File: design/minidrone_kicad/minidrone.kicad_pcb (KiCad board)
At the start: 2 copper layers, 40.6 x 73.7 mm, 34 parts, among them J1 programming, J2 HM-13 Bluetooth, J3 BAT, J4 mpu6050, J5 FL Motor, J6 BL Motor, J7 FR Motor, J8 BR Motor, Q1 SI2302, Q2 SI2302, Q3 SI2302, Q4 SI2302, U1 stm32_BluePill

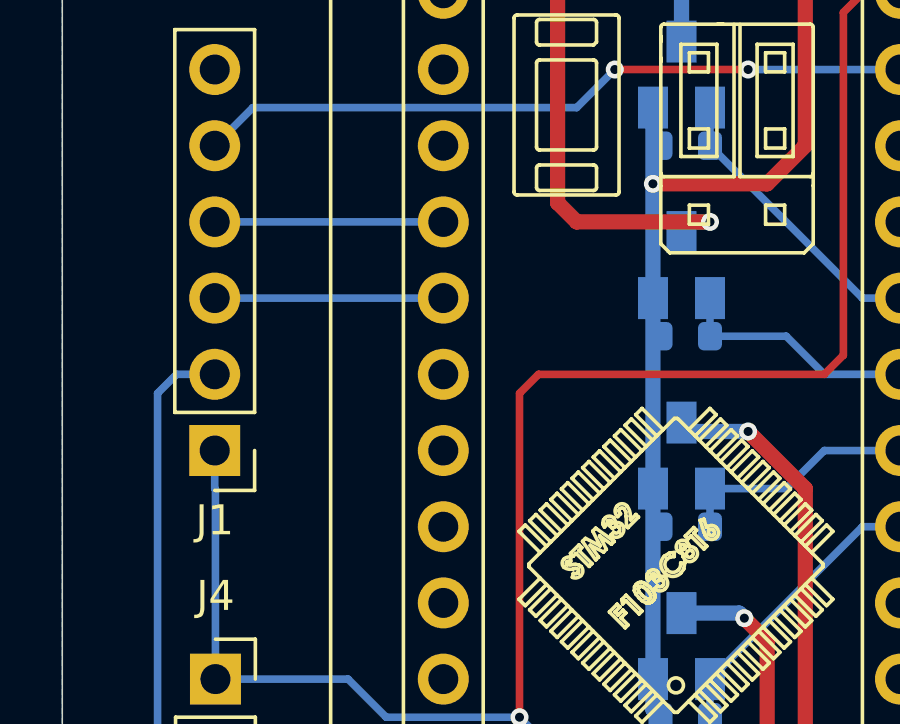
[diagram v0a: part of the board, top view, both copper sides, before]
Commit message: fix(PCH/PCB): Programming pins and motor pins definition.
Correct the programming TX/RX connection.
Update the motor net-names due to the design changed.
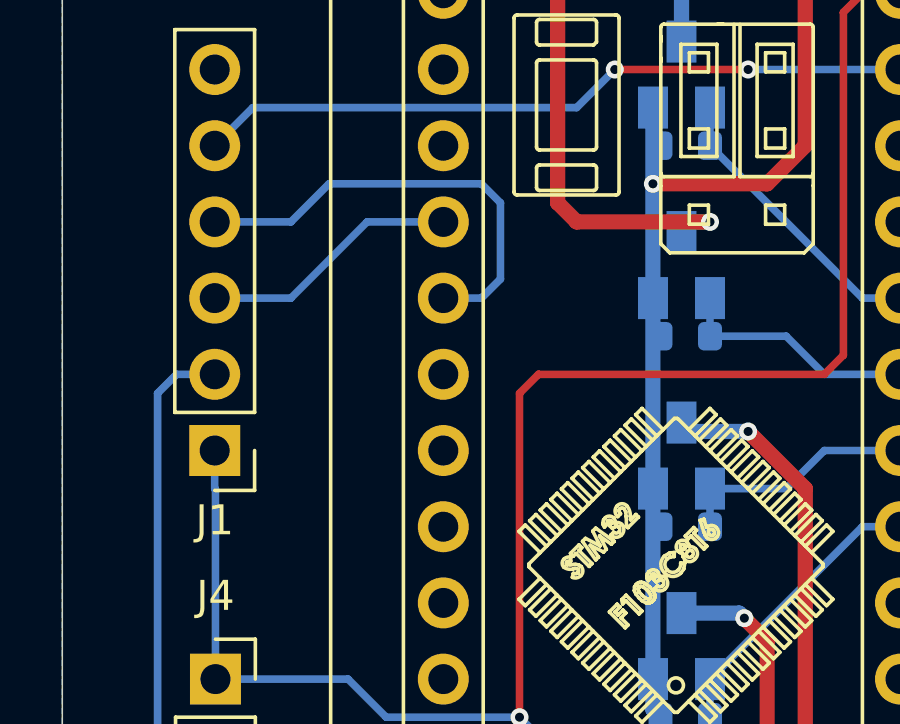
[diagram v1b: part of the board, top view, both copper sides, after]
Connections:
- J1 pad 3: /PRG_TX -> /PRG_RX
- J1 pad 4: /PRG_RX -> /PRG_TX
- Q1 pad 1: /FL_PWM -> /BR_PWM
- Q2 pad 1: /BL_PWM -> /FR_PWM
- Q3 pad 1: /FR_PWM -> /BL_PWM
- Q4 pad 1: /BR_PWM -> /FL_PWM
- R10 pad 1: /FR_PWM -> /BL_PWM
- R11 pad 1: /BR_PWM -> /FL_PWM
- R8 pad 1: /FL_PWM -> /BR_PWM
- R9 pad 1: /BL_PWM -> /FR_PWM
- U1 pad 31: /BL_PWM -> /FR_PWM
- U1 pad 32: /FR_PWM -> /BL_PWM
- U1 pad 33: /FL_PWM -> /BR_PWM
- U1 pad 34: /BR_PWM -> /FL_PWM
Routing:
- net /PRG_TX: track 7.62 -> 15.0 mm
- net /FL_PWM: track 8.15 -> 9.72 mm
- net /BR_PWM: track 9.72 -> 8.15 mm
- net /FR_PWM: track 8.15 -> 9.72 mm
- net /BL_PWM: track 9.72 -> 8.15 mm
- net /PRG_RX: track 7.62 -> 8.67 mm

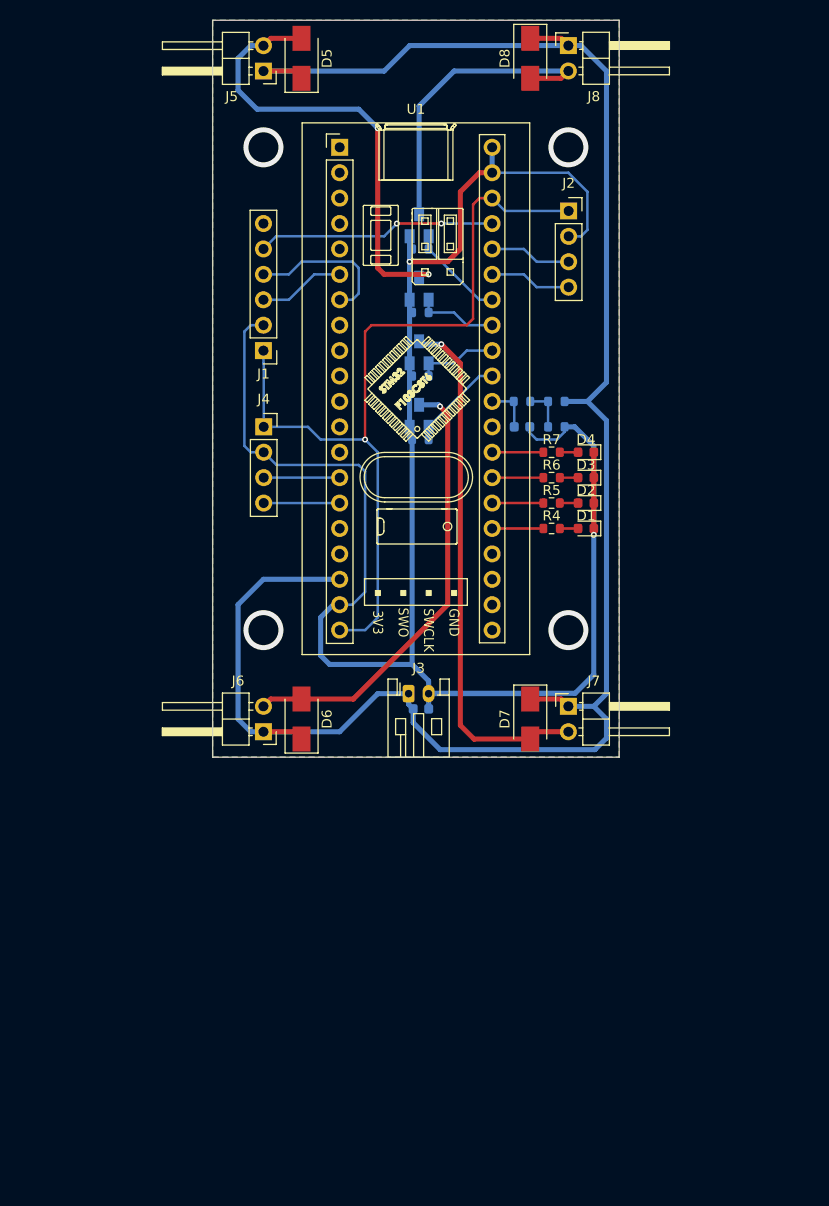
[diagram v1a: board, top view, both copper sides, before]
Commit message: docs(SCH/PCB): Update the PCB design to v2.
The v1's handmade version is too heavy.
 - Remove the STM32 blue pill board.
 - Using the STM32F103CBT6 to make sure the ROM size enough.
 - Design the PCB as the drone's frame.
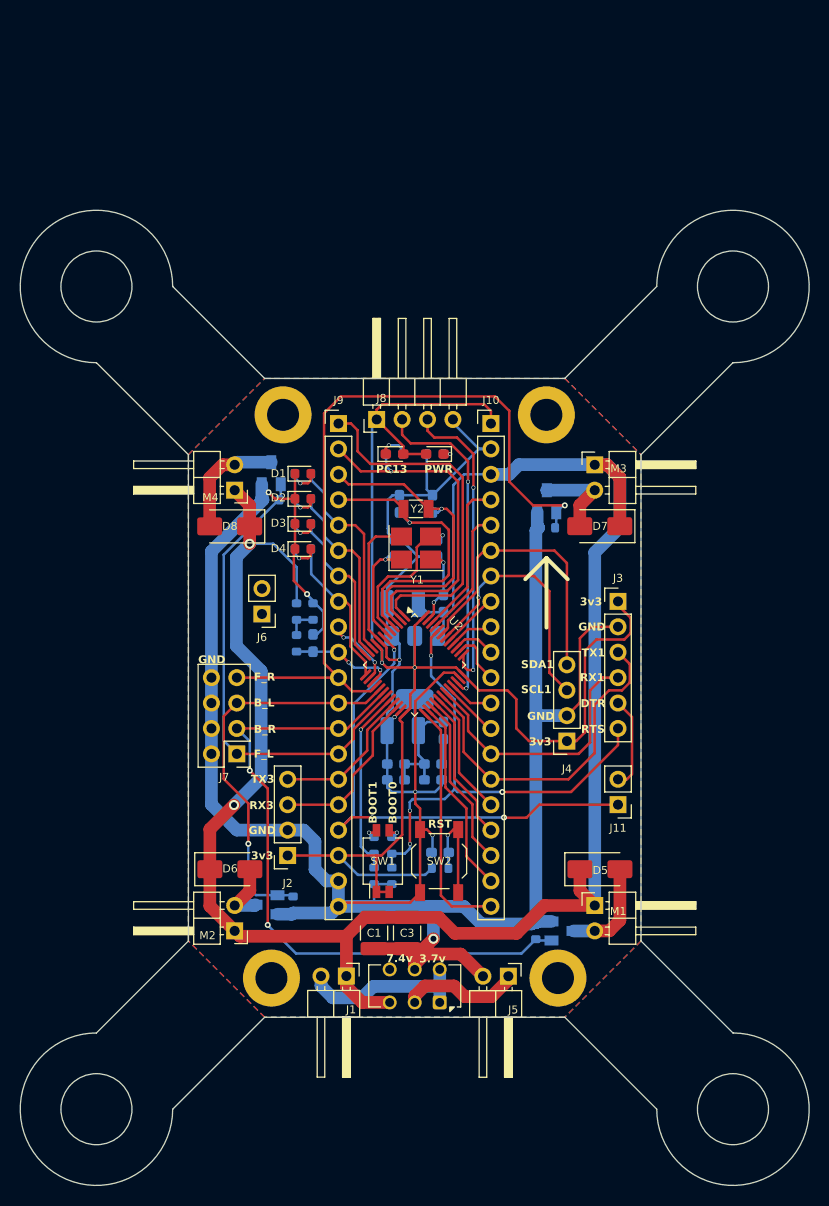
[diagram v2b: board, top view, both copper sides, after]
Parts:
- added ?: , , F.Cu at (135.7, 131.5)
- added ?: , , F.Cu at (163.3, 75.0)
- added ?: , , F.Cu at (164.3, 131.3)
- added C10: 0.1 uF, Capacitor_SMD:C_0603_1608Metric_Pad1.08x0.95mm_HandSolder, B.Cu at (148.1, 111.5)
- added C11: 0.1 uF, Capacitor_SMD:C_0603_1608Metric_Pad1.08x0.95mm_HandSolder, B.Cu at (151.8, 111.5)
- added C12: 0.1 uF, Capacitor_SMD:C_0603_1608Metric_Pad1.08x0.95mm_HandSolder, B.Cu at (151.8, 109.9)
- added C13: 20 pF, Capacitor_SMD:C_0603_1608Metric_Pad1.08x0.95mm_HandSolder, B.Cu at (152.3, 88.3)
- added C14: 12 pF, Capacitor_SMD:C_0603_1608Metric_Pad1.08x0.95mm_HandSolder, B.Cu at (151.8, 83.9)
- added C15: 20 pF, Capacitor_SMD:C_0603_1608Metric_Pad1.08x0.95mm_HandSolder, B.Cu at (148.0, 88.3)
- added C16: 12 pF, Capacitor_SMD:C_0603_1608Metric_Pad1.08x0.95mm_HandSolder, B.Cu at (148.5, 83.9)
- added C3: 10 uF, Capacitor_SMD:C_1210_3225Metric_Pad1.33x2.70mm_HandSolder, F.Cu at (149.2, 126.8)
- added C4: 10 uF, Capacitor_SMD:C_1210_3225Metric_Pad1.33x2.70mm_HandSolder, B.Cu at (148.8, 93.9)
- added C5: 0.1 uF, Capacitor_SMD:C_0603_1608Metric_Pad1.08x0.95mm_HandSolder, B.Cu at (152.9, 93.9)
- added C6: 10 uF, Capacitor_SMD:C_1210_3225Metric_Pad1.33x2.70mm_HandSolder, B.Cu at (148.8, 106.6)
- added C7: 0.1 uF, Capacitor_SMD:C_0603_1608Metric_Pad1.08x0.95mm_HandSolder, B.Cu at (152.9, 106.6)
- added C8: 1 uF, Capacitor_SMD:C_0603_1608Metric_Pad1.08x0.95mm_HandSolder, B.Cu at (152.5, 118.7)
- added C9: 0.1 uF, Capacitor_SMD:C_0603_1608Metric_Pad1.08x0.95mm_HandSolder, B.Cu at (148.1, 109.9)
- added D10: LED, LED_SMD:LED_0603_1608Metric_Pad1.05x0.95mm_HandSolder, F.Cu at (148.0, 78.9)
- added D9: LED, LED_SMD:LED_0603_1608Metric_Pad1.05x0.95mm_HandSolder, F.Cu at (152.0, 78.9)
- added J10: Conn_01x20, Connector_PinHeader_2.54mm:PinHeader_1x20_P2.54mm_Vertical, F.Cu at (157.6, 75.9)
- added J11: jumper, Connector_PinHeader_2.54mm:PinHeader_1x02_P2.54mm_Vertical, F.Cu at (170.3, 114.0)
- added J9: Conn_01x20, Connector_PinHeader_2.54mm:PinHeader_1x20_P2.54mm_Vertical, F.Cu at (142.4, 75.9)
- added M1: BR, Connector_PinHeader_2.54mm:PinHeader_1x02_P2.54mm_Horizontal, F.Cu at (168.0, 124.0)
- added M2: BL, Connector_PinHeader_2.54mm:PinHeader_1x02_P2.54mm_Horizontal, F.Cu at (132.0, 126.6)
- added M3: FR, Connector_PinHeader_2.54mm:PinHeader_1x02_P2.54mm_Horizontal, F.Cu at (168.0, 80.0)
- added M4: FL, Connector_PinHeader_2.54mm:PinHeader_1x02_P2.54mm_Horizontal, F.Cu at (132.0, 82.5)
- added R12: 10 K, Resistor_SMD:R_0603_1608Metric, B.Cu at (152.5, 120.3)
- added R13: 1 K, Resistor_SMD:R_0603_1608Metric, B.Cu at (152.0, 78.9)
- added R14: 10 K, Resistor_SMD:R_0603_1608Metric, B.Cu at (147.7, 118.0)
- added R15: 10 K, Resistor_SMD:R_0603_1608Metric, B.Cu at (145.9, 118.0)
- added R16: 1 K, Resistor_SMD:R_0603_1608Metric, B.Cu at (148.0, 78.9)
- added R17: 100 K, Resistor_SMD:R_0603_1608Metric, B.Cu at (147.7, 121.1)
- added R18: 100 K, Resistor_SMD:R_0603_1608Metric, B.Cu at (145.9, 121.1)
- added REF**: MountingHole_3.2mm_M3_ISO7380_Pad, MountingHole:MountingHole_3.2mm_M3_ISO7380_Pad, F.Cu at (136.8, 75.0)
- added SW1: SW_DIP_x02, Button_Switch_SMD:SW_DIP_SPSTx02_Slide_Omron_A6H-2101_W6.15mm_P1.27mm, F.Cu at (146.8, 119.6)
- added SW2: SW_Push, Button_Switch_SMD:SW_SPST_TL3342, F.Cu at (152.4, 119.6)
- added SW3: V_sw, Button_Switch_THT:SW_CK_JS202011CQN_DPDT_Straight, F.Cu at (152.5, 133.7)
- added U2: STM32F103CBTx, Package_QFP:LQFP-48_7x7mm_P0.5mm, F.Cu at (150.0, 100.0)
- added Y1: 8MHz, Crystal:Crystal_SMD_3225-4Pin_3.2x2.5mm_HandSoldering, F.Cu at (150.1, 88.3)
- added Y2: 32,768KHz, Crystal:Crystal_SMD_3215-2Pin_3.2x1.5mm, F.Cu at (150.1, 84.4)
- C1: value 104p -> 10 uF; footprint Capacitor_SMD:C_0603_1608Metric -> Capacitor_SMD:C_1210_3225Metric_Pad1.33x2.70mm_HandSolder; moved to F.Cu
- C2: value 103p -> 0.1 uF; footprint Capacitor_SMD:C_0603_1608Metric -> Capacitor_SMD:C_0603_1608Metric_Pad1.08x0.95mm_HandSolder
- J1: value programming -> BAT; footprint Connector_PinHeader_2.54mm:PinHeader_1x06_P2.54mm_Vertical -> Connector_PinHeader_2.54mm:PinHeader_1x02_P2.54mm_Horizontal
- J3: value BAT -> programming; footprint Connector_JST:JST_PH_S2B-PH-K_1x02_P2.00mm_Horizontal -> Connector_PinHeader_2.54mm:PinHeader_1x06_P2.54mm_Vertical
- J5: value FL Motor -> BAT
- J6: value BL Motor -> place_holder; footprint Connector_PinHeader_2.54mm:PinHeader_1x02_P2.54mm_Horizontal -> Connector_PinHeader_2.54mm:PinHeader_1x02_P2.54mm_Vertical
- J7: value FR Motor -> Conn_02x04_Odd_Even; footprint Connector_PinHeader_2.54mm:PinHeader_1x02_P2.54mm_Horizontal -> Connector_PinHeader_2.54mm:PinHeader_2x04_P2.54mm_Vertical
- J8: value BR Motor -> J-Link; footprint Connector_PinHeader_2.54mm:PinHeader_1x02_P2.54mm_Horizontal -> Connector_PinHeader_2.54mm:PinHeader_1x04_P2.54mm_Horizontal
- R1: value 20 K -> 30 K
- R2, R3: value 30 K -> 180
- R4, R5: moved to B.Cu
- R6: value 180 -> 30 K; moved to B.Cu
- R7: value 180 -> 10 K; moved to B.Cu
- U1: value stm32_BluePill -> LM1117MP-3.3; footprint STM32_module:stm32_BluePill_1 -> Package_TO_SOT_SMD:SOT-223-3_TabPin2; moved to B.Cu
- moved J5 93.7 mm to (159.4, 131.1), turned to -90 degrees
- moved D5 86.4 mm to (168.5, 120.4), turned to 0 degrees
- moved J2 70.3 mm to (137.3, 119.0), turned to 180 degrees
- moved Q1 65.8 mm to (164.8, 126.6), turned to 90 degrees
- moved J1 63.1 mm to (143.2, 131.1), turned to -90 degrees
- moved R8 62.9 mm to (162.1, 126.6), turned to 90 degrees
- moved D8 55.6 mm to (131.5, 86.2), turned to 180 degrees
- moved U1 52.5 mm to (150.0, 100.3), turned to -90 degrees
- moved Q2 51.2 mm to (135.2, 124.0), turned to -90 degrees
- moved R9 48.2 mm to (137.8, 124.0), turned to -90 degrees
- moved J4 43.6 mm to (165.2, 107.6), turned to 180 degrees
- moved J8 42.0 mm to (146.2, 75.5), turned to 90 degrees
- moved J7 33.5 mm to (132.2, 108.9), turned to 180 degrees
- moved R1 33.4 mm to (138.2, 94.7), turned to -90 degrees
- moved R6 30.4 mm to (138.2, 97.8), turned to -90 degrees
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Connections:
- C2 pad 1: /VBAT -> /VBAT_a
- J1 pad 1: +3.3V -> +BATT
- J1 pad 2: GND -> Net-(J1-Pin_2)
- J3 pad 1: +BATT -> +3.3V
- J5 pad 1: +BATT -> Net-(J5-Pin_1)
- J5 pad 2: Net-(D5-A) -> GND
- J6 pad 1: +BATT -> unconnected-(J6-Pin_1-Pad1)
- J6 pad 2: Net-(D6-A) -> unconnected-(J6-Pin_2-Pad2)
- J7 pad 1: +BATT -> /FL_PWM
- J7 pad 2: Net-(D7-A) -> GND
- J8 pad 1: +BATT -> +3.3V
- J8 pad 2: Net-(D8-A) -> /stm32_dev/SWDIO
- Q2 pad 1: /FR_PWM -> /BL_PWM
- Q3 pad 1: /BL_PWM -> /FR_PWM
- R10 pad 1: /BL_PWM -> /FR_PWM
- R2 pad 1: Net-(R1-Pad2) -> /STAT_0
- R2 pad 2: GND -> Net-(D1-A)
- R3 pad 1: Net-(R1-Pad2) -> /STAT_1
- R3 pad 2: /VBAT -> Net-(D2-A)
- R4 pad 1: /STAT_0 -> /STAT_2
- R4 pad 2: Net-(D1-A) -> Net-(D3-A)
- R5 pad 1: /STAT_1 -> /STAT_3
- R5 pad 2: Net-(D2-A) -> Net-(D4-A)
- R6 pad 1: /STAT_2 -> Net-(R1-Pad2)
- R6 pad 2: Net-(D3-A) -> /VBAT_a
- R7 pad 1: /STAT_3 -> Net-(R1-Pad2)
- R7 pad 2: Net-(D4-A) -> GND
- R9 pad 1: /FR_PWM -> /BL_PWM
- U1 pad 1: unconnected-(U1-PB12-Pad1) -> GND
- U1 pad 2: unconnected-(U1-PB13-Pad2) -> +3.3V
- U1 pad 3: unconnected-(U1-PB14-Pad3) -> +BATT
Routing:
- net GND: track 214.0 -> 317.1 mm, vias 6 -> 9
- net +3.3V: track 84.8 -> 160.7 mm, vias 1 -> 2
- net /FR_PWM: track 9.72 -> 77.7 mm, vias 0 -> 1
- net /BR_PWM: track 8.15 -> 67.1 mm, vias 0 -> 2
- net /stm32_dev/RST: track 0.00 -> 51.1 mm, vias 0 -> 3
- net /PRG_RTS: track 0.00 -> 50.3 mm, vias 0 -> 4
- net Net-(D7-A): track 52.9 -> 9.01 mm, vias 1 -> 0
- net Net-(D6-A): track 44.9 -> 6.34 mm, vias 1 -> 0
- net /FL_PWM: track 9.72 -> 47.6 mm
- net Net-(D5-A): track 46.3 -> 10.2 mm, vias 2 -> 0
- net /stm32_dev/VBAT: track 0.00 -> 35.8 mm
- net /stm32_dev/PC13: track 0.00 -> 35.1 mm, vias 0 -> 1
- net /stm32_dev/SWDIO: track 0.00 -> 33.2 mm, vias 0 -> 2
- net /BL_PWM: track 8.15 -> 39.5 mm, vias 0 -> 1
- net /stm32_dev/PC14: track 0.00 -> 31.3 mm, vias 0 -> 1
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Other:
- board size 40.6 x 73.7 mm -> 78.9 x 97.5 mm
- board text added: "3.7v"
- board text added: "3v3"
- board text added: "7.4v"
- board text added: "BOOT0"
- board text added: "BOOT1"
- board text added: "B_L"
- board text added: "B_R"
- board text added: "DTR"
- board text added: "F_L"
- board text added: "F_R"
- board text added: "GND"
- board text added: "PC13"
- board text added: "PWR"
- board text added: "RST"
- board text added: "RTS"
- board text added: "RX1"
- board text added: "RX3"
- board text added: "SCL1"
- board text added: "SDA1"
- board text added: "TX1"
- board text added: "TX3"

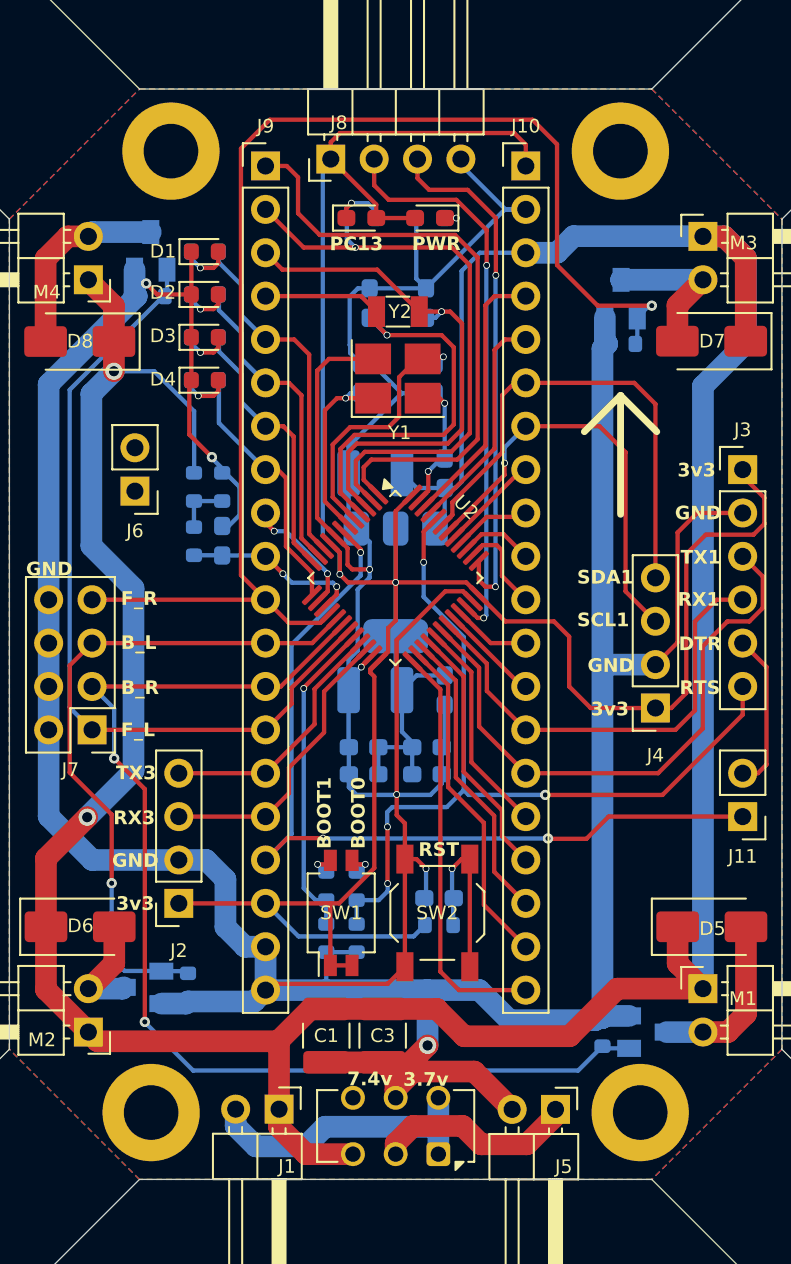
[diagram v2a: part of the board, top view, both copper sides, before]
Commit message: fix(SCH/PCB): The reset button no function
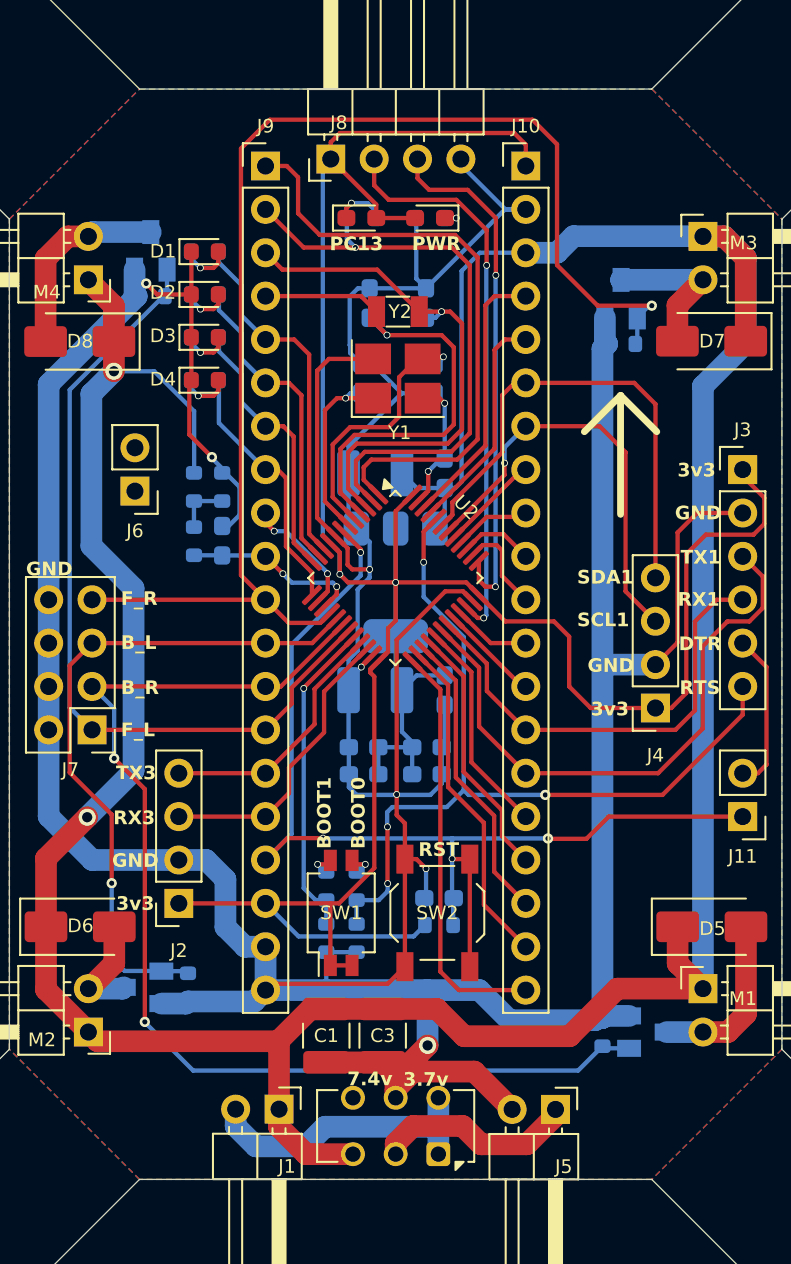
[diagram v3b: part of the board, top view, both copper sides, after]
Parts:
- removed ? (x3): , 
- removed REF**: MountingHole_3.2mm_M3_ISO7380_Pad, MountingHole:MountingHole_3.2mm_M3_ISO7380_Pad
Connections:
- C8 pad 1: Net-(C8-Pad1) -> /stm32_dev/Reset
- J11 pad 1: /stm32_dev/RST -> /stm32_dev/Reset
- J9 pad 17: /stm32_dev/RST -> /stm32_dev/Reset
- R12 pad 2: Net-(C8-Pad1) -> /stm32_dev/Reset
- SW2 pad 2: Net-(C8-Pad1) -> /stm32_dev/Reset
- U2 pad 7: /stm32_dev/RST -> /stm32_dev/Reset
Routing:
- net /stm32_dev/Reset: track 0.00 -> 63.4 mm, vias 0 -> 4
- net /stm32_dev/RST: track 51.1 -> 0.00 mm, vias 3 -> 0
- net Net-(C8-Pad1): track 10.7 -> 0.00 mm, vias 1 -> 0

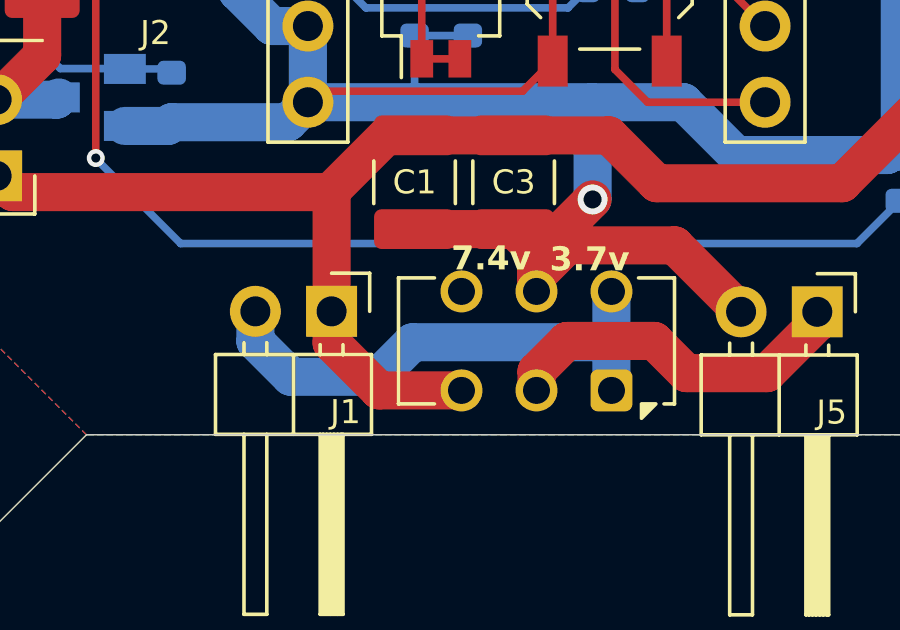
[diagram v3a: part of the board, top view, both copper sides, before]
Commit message: fix(circuit): fix the battery series or parallel circuits
- Correct the invert connection on SW3
- Correct the silkscreen for voltage selection
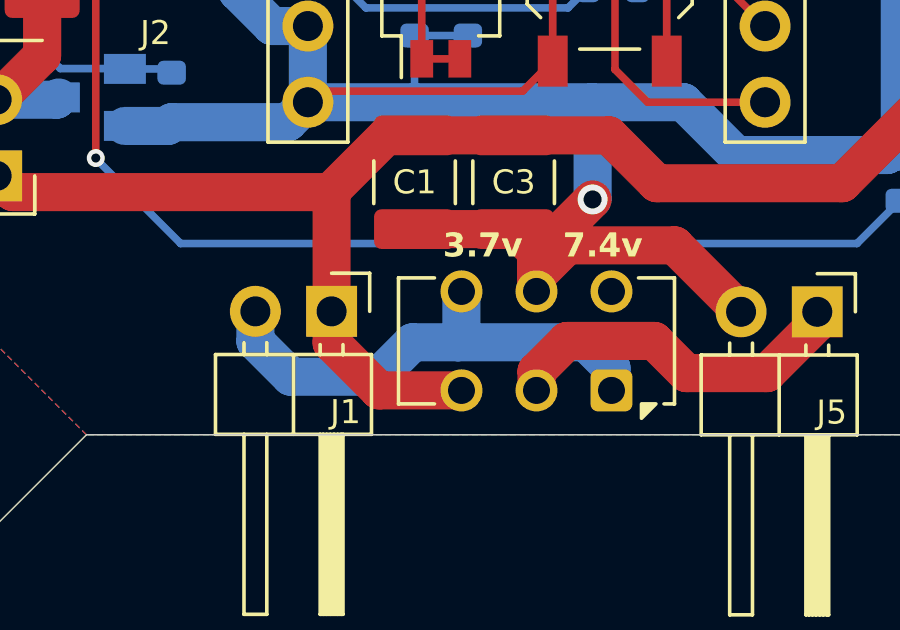
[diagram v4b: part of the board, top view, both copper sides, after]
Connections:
- SW3 pad 4: unconnected-(SW3B-A-Pad4) -> Net-(J1-Pin_2)
- SW3 pad 6: Net-(J1-Pin_2) -> unconnected-(SW3B-C-Pad6)

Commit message: fix(circuit): add mounting hole
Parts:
- added H1: Pad, MountingHole:MountingHole_3.2mm_M3_ISO7380_Pad_TopBottom, F.Cu at (135.9, 74.9)
- added H2: Pad, MountingHole:MountingHole_3.2mm_M3_ISO7380_Pad_TopBottom, F.Cu at (163.9, 74.9)
- added H3: Pad, MountingHole:MountingHole_3.2mm_M3_ISO7380_Pad_TopBottom, F.Cu at (135.4, 131.4)
- added H4: Pad, MountingHole:MountingHole_3.2mm_M3_ISO7380_Pad_TopBottom, F.Cu at (164.4, 131.4)
